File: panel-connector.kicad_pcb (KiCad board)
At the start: 2 copper layers, 95.9 x 90.2 mm, 25 parts, among them J1 PC104-8BIT, J10 CONN-TAB, J11 MOLEX_FFC-14, J12 CONN-TAB, J13 CONN-TAB, J14 CONN-TAB, J15 CONN-TAB, J16 MOLEX_FFC-14, J17 CONN-TAB, J18 CONN-TAB, J19 CONN-TAB, J2 PC104PTH, J20 CONN-TAB, J21 MOLEX_FFC-14, J22 CONN-TAB, J23 CONN-TAB, J24 CONN-TAB, J25 CONN-TAB, J3 PC104PTH, J4 PC104PTH, J5 PC104PTH, J6 MOLEX_FFC-14, J7 CONN-TAB, J8 CONN-TAB, J9 CONN-TAB

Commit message: Added mux
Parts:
- added 0.1uF1, 0.1uF2, 0.1uF3, 0.1uF4, C1, C2, C3, C4: C, Capacitors_SMD:C_0402, F.Cu at (55.9, 110.1)
- added R1, R10, R11, R12, R13, R14, R15, R16, R17, R18, R19, R2, R20, R23, R24, R27, R28, R3, R31, R32, R4, R5, R6, R7, R8, R9: R, Resistors_SMD:R_0402, F.Cu at (55.9, 110.1)
- added U1: ADG728, SFUSat:TSSOP-16, F.Cu at (39.7, 95.3)
- added U2: ADG728, SFUSat:TSSOP-16, F.Cu at (47.7, 95.3)
- added U3: ADG728, SFUSat:TSSOP-16, F.Cu at (55.7, 95.3)
- added U4: ADG728, SFUSat:TSSOP-16, F.Cu at (64.0, 95.3)

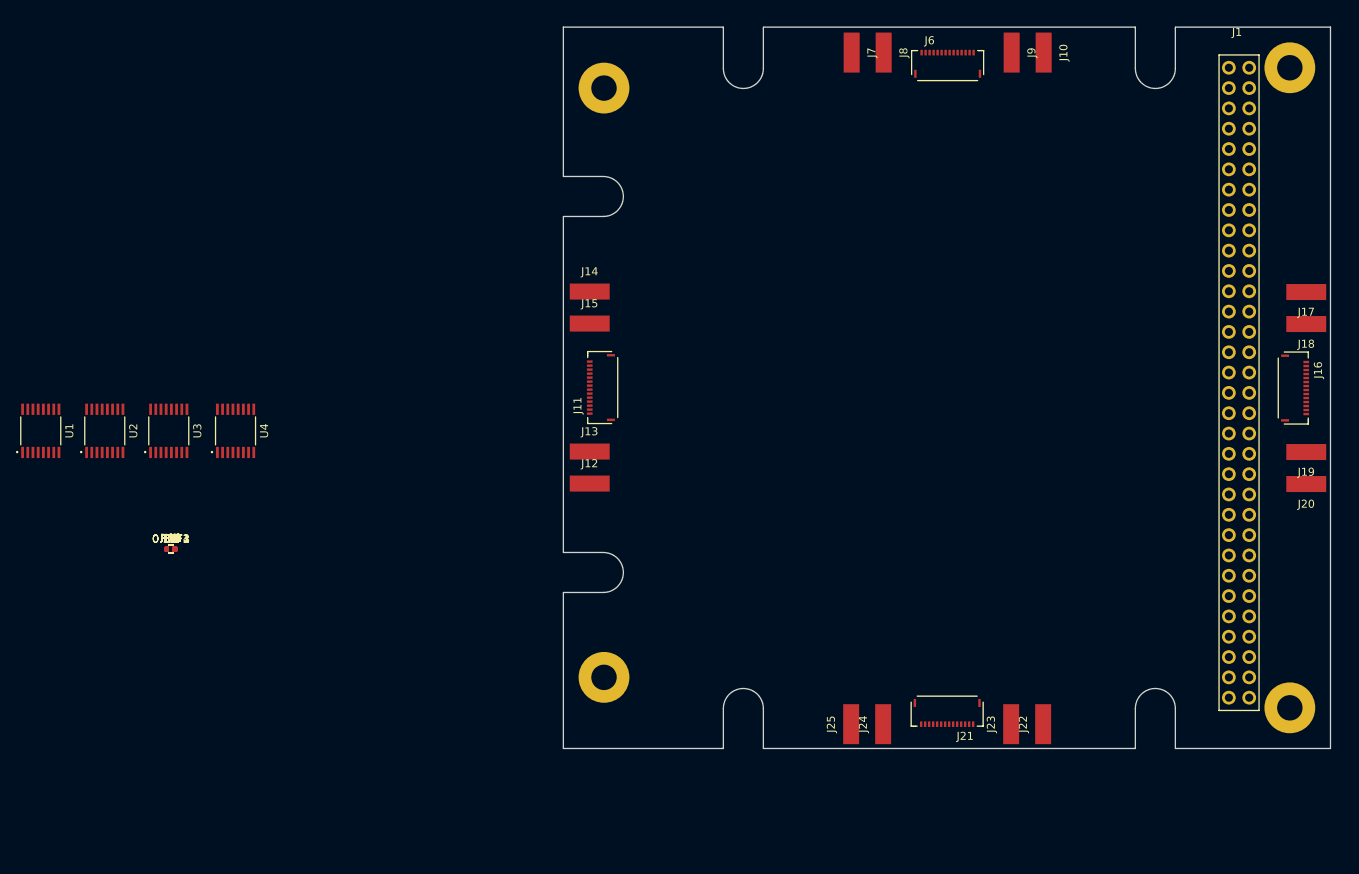
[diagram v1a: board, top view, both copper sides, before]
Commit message: Assigned some footprints and connected some nets
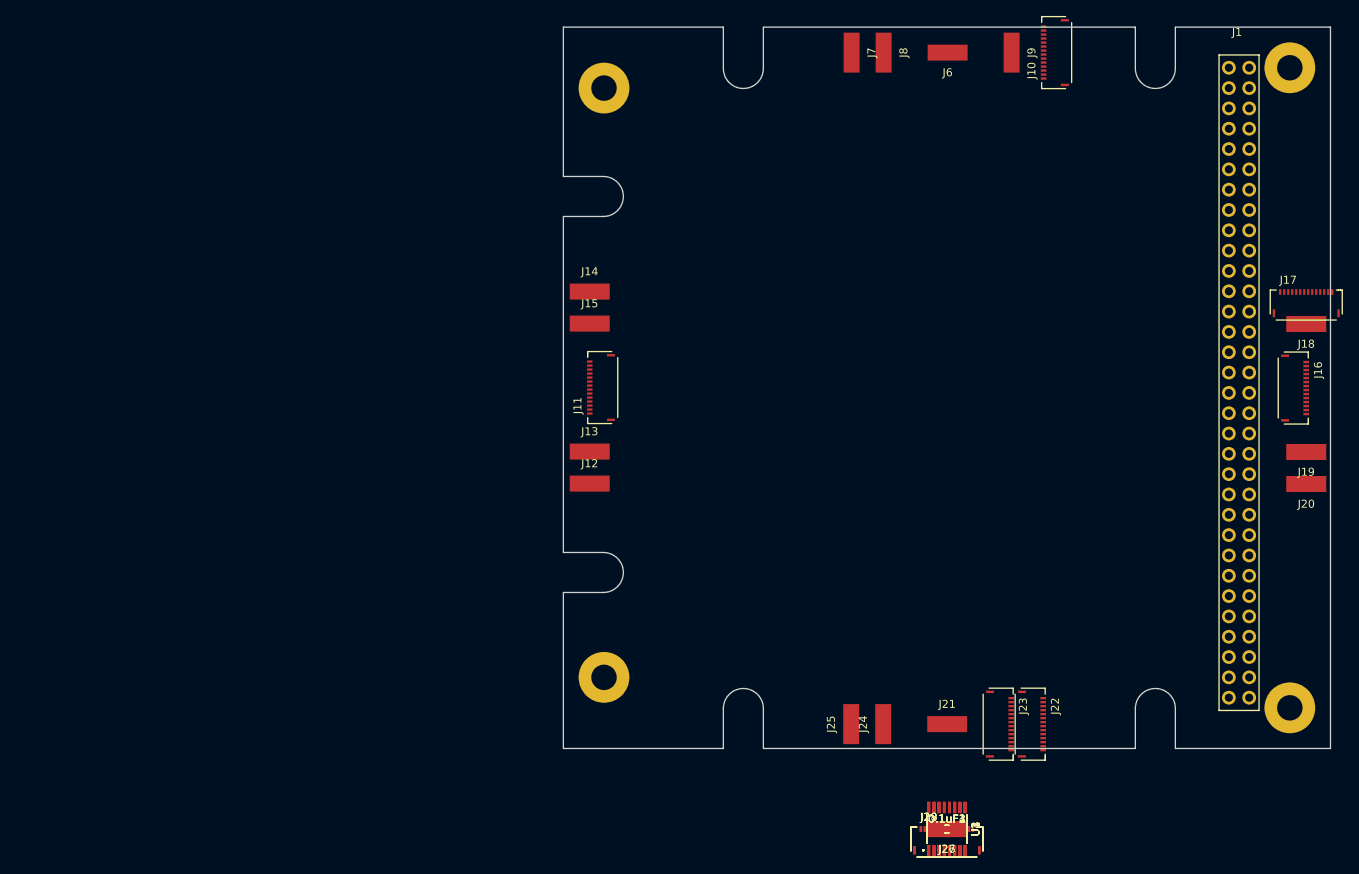
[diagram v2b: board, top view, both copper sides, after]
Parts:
- removed C1, C2, C3, C4: C, Capacitors_SMD:C_0402
- removed R1, R10, R11, R12, R13, R14, R15, R16, R17, R18, R19, R2, R20, R23, R24, R27, R28, R3, R31, R32, R4, R5, R6, R7, R8, R9: R, Resistors_SMD:R_0402
- added J26, J27: CONN-TAB, SFUSat:CONN_TAB, F.Cu at (152.9, 145.1)
- added J28, J29: MOLEX_FFC-14, SFUSat:MOLEX_FFC-14, F.Cu at (152.9, 145.1)
- J10, J17, J22, J23: value CONN-TAB -> MOLEX_FFC-14; footprint SFUSat:CONN_TAB -> SFUSat:MOLEX_FFC-14
- J21, J6: value MOLEX_FFC-14 -> CONN-TAB; footprint SFUSat:MOLEX_FFC-14 -> SFUSat:CONN_TAB
- moved U1 123.7 mm to (152.9, 145.1)
- moved U2 116.4 mm to (152.9, 145.1)
- moved U3 109.3 mm to (152.9, 145.1)
- moved 0.1uF1 103.1 mm to (152.9, 145.1)
- moved 0.1uF2 103.1 mm to (152.9, 145.1)
- moved 0.1uF3 103.1 mm to (152.9, 145.1)
- moved 0.1uF4 103.1 mm to (152.9, 145.1)
- moved U4 101.9 mm to (152.9, 145.1)

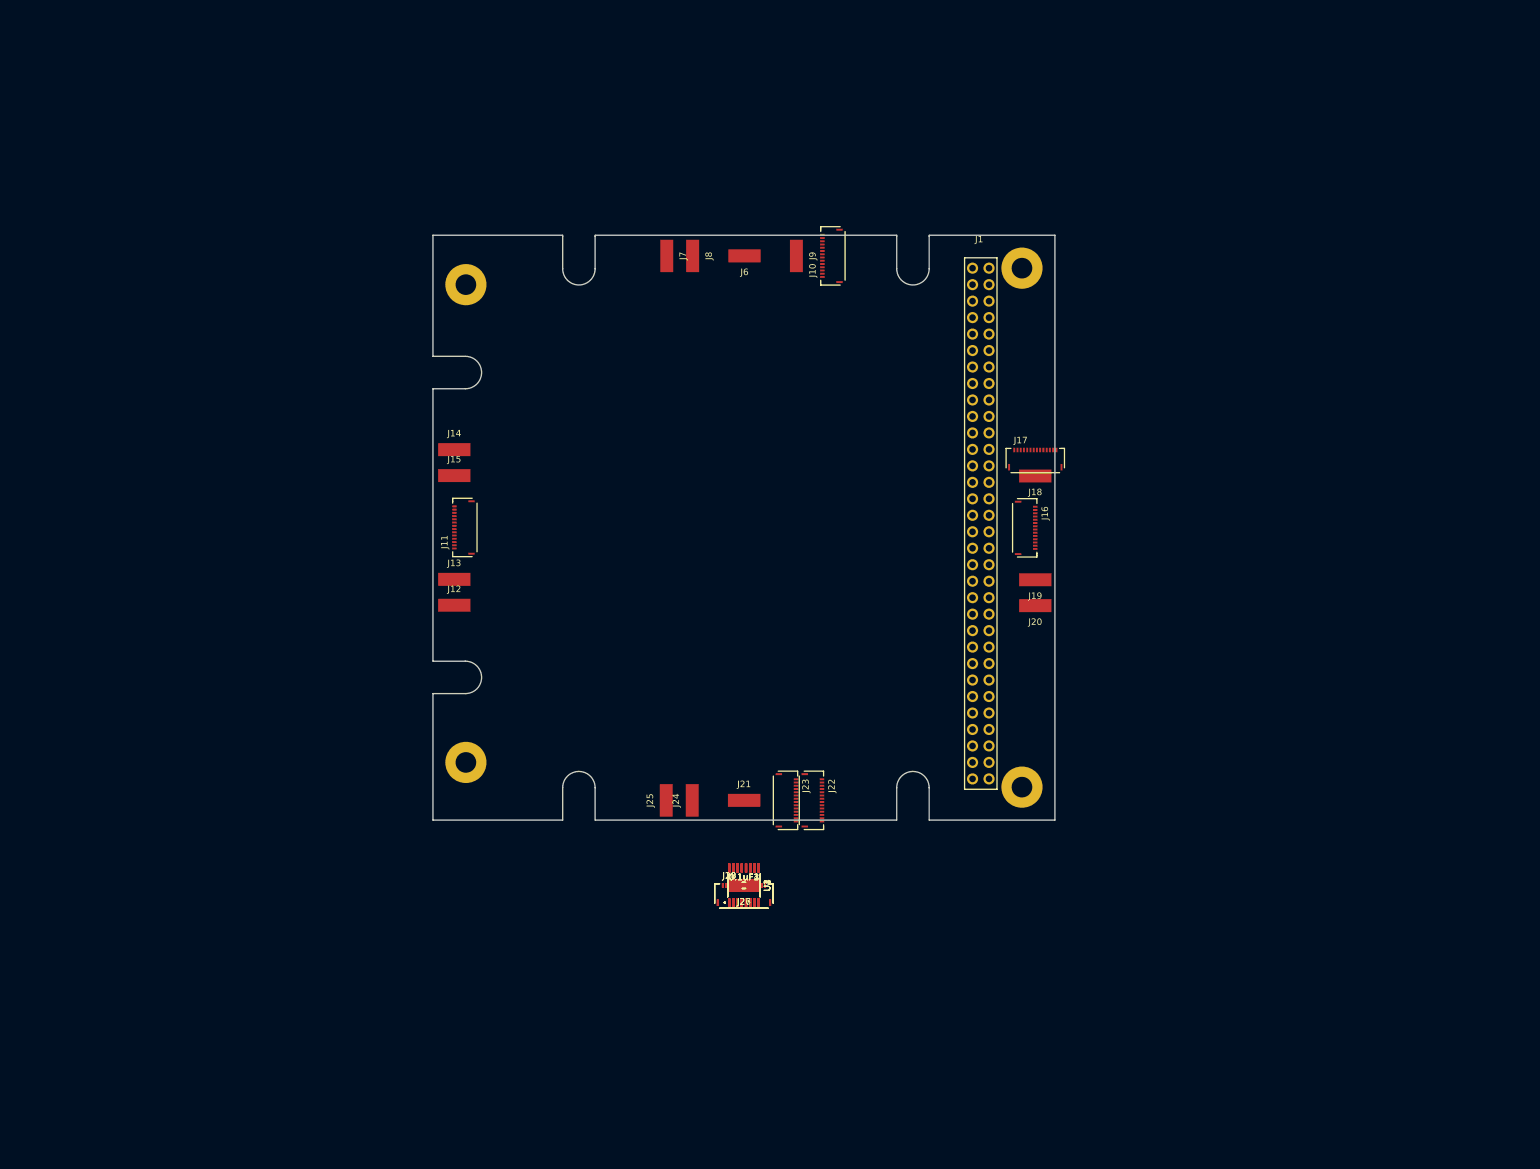
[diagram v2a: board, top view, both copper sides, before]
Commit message: Begand layout of connectors and added 3d models. The +Z connector will be placed only on the -X side of the board but because of the schematic hierarchy the net shows it is connected to all sides; ignore that for now. Connnected the sun sensor connector to mux according to systems spreadsheet, orientation does need checking.
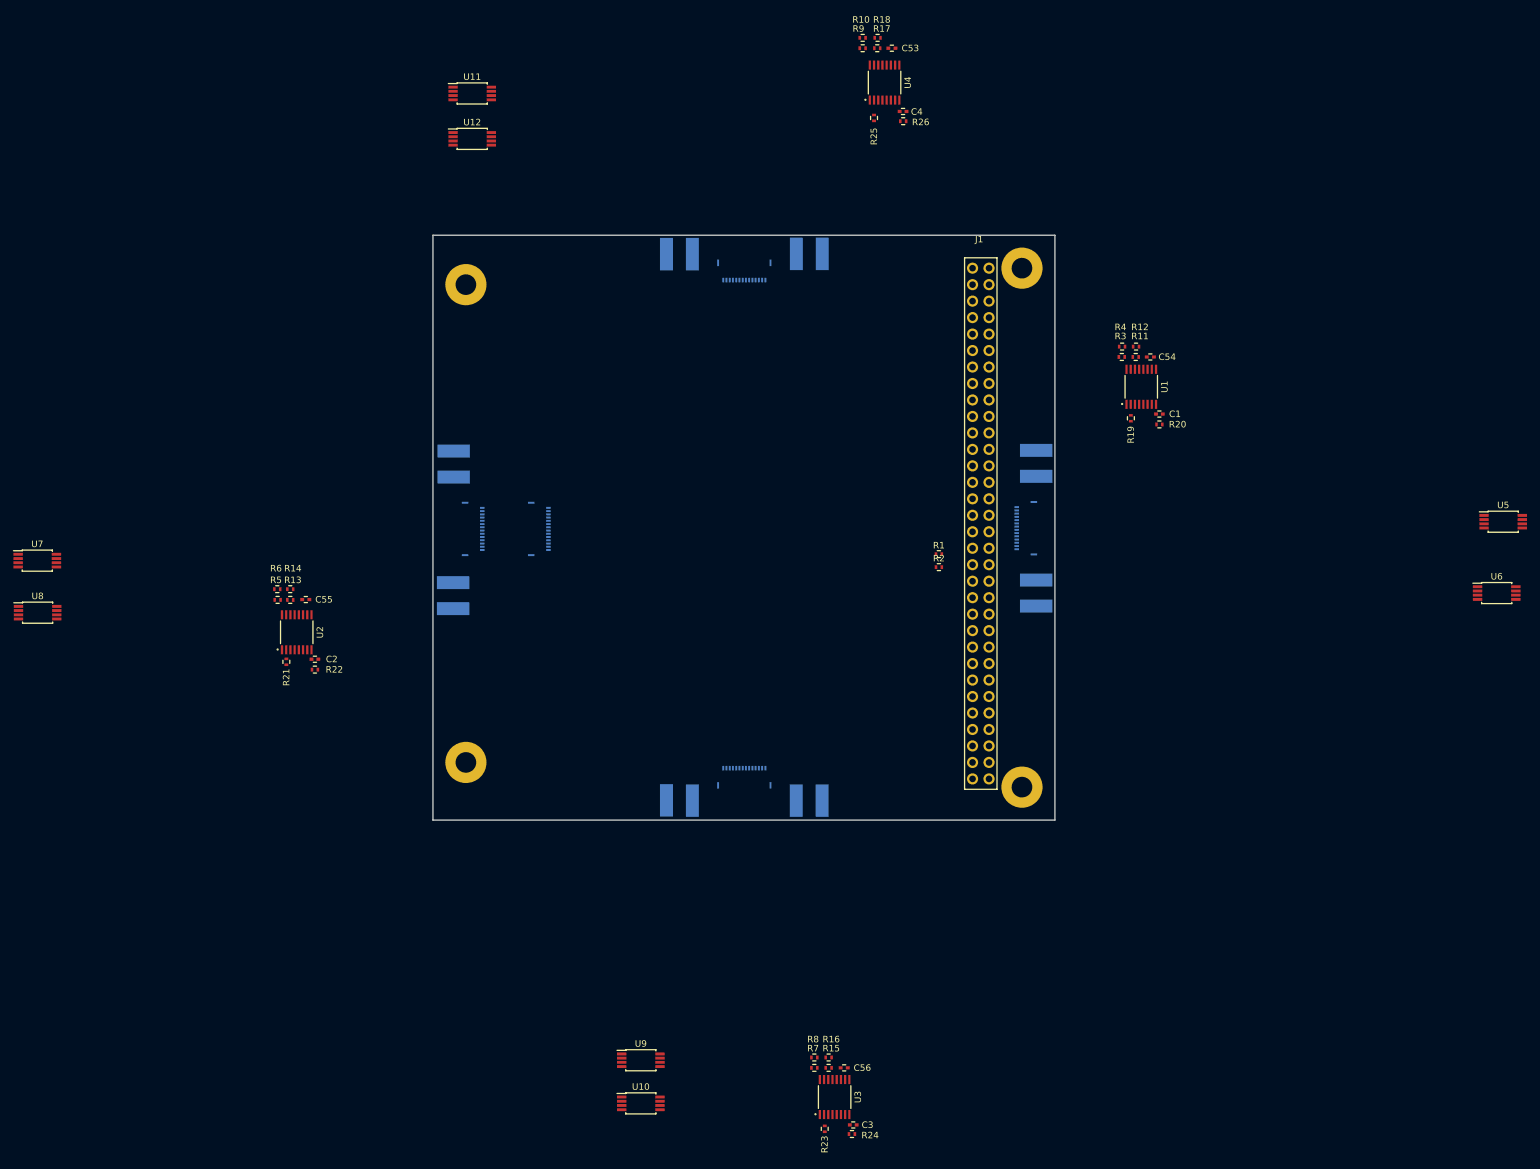
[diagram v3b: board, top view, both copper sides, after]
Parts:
- removed 0.1uF1, 0.1uF2, 0.1uF3, 0.1uF4: C, Capacitors_SMD:C_0402
- removed J17, J23, J29: MOLEX_FFC-14, SFUSat:MOLEX_FFC-14
- added C1: DNP, SFUSat:C_0402, F.Cu at (217.0, 72.4)
- added C2: DNP, SFUSat:C_0402, F.Cu at (86.8, 110.2)
- added C3: DNP, SFUSat:C_0402, F.Cu at (169.8, 182.0)
- added C4: DNP, SFUSat:C_0402, F.Cu at (177.5, 25.8)
- added C53: DNP, Capacitors_SMD:C_0402, F.Cu at (175.8, 16.0)
- added C54: DNP, Capacitors_SMD:C_0402, F.Cu at (215.6, 63.6)
- added C55: DNP, Capacitors_SMD:C_0402, F.Cu at (85.4, 101.0)
- added C56: DNP, Capacitors_SMD:C_0402, F.Cu at (168.4, 173.2)
- added R1: R, SFUSat:R_0402, F.Cu at (183.0, 94.0)
- added R10: DNP, SFUSat:R_0402, F.Cu at (171.2, 14.4)
- added R11: DNP, SFUSat:R_0402, F.Cu at (213.3, 63.6)
- added R12: 0R, SFUSat:R_0402, F.Cu at (213.4, 62.0)
- added R13: DNP, SFUSat:R_0402, F.Cu at (83.0, 101.0)
- added R14: 0R, SFUSat:R_0402, F.Cu at (83.0, 99.4)
- added R15: 0R, SFUSat:R_0402, F.Cu at (166.0, 173.2)
- added R16: DNP, SFUSat:R_0402, F.Cu at (166.0, 171.6)
- added R17: 0R, SFUSat:R_0402, F.Cu at (173.5, 16.0)
- added R18: DNP, SFUSat:R_0402, F.Cu at (173.6, 14.4)
- added R19: R, SFUSat:R_0402, F.Cu at (212.6, 73.0)
- added R2: R, SFUSat:R_0402, F.Cu at (183.0, 96.0)
- added R20: DNP, SFUSat:R_0402, F.Cu at (217.0, 74.0)
- added R21: R, SFUSat:R_0402, F.Cu at (82.4, 110.6)
- added R22: DNP, SFUSat:R_0402, F.Cu at (86.8, 111.8)
- added R23: R, SFUSat:R_0402, F.Cu at (165.4, 182.6)
- added R24: DNP, SFUSat:R_0402, F.Cu at (169.6, 183.4)
- added R25: R, SFUSat:R_0402, F.Cu at (173.0, 26.8)
- added R26: DNP, SFUSat:R_0402, F.Cu at (177.5, 27.2)
- added R3: DNP, SFUSat:R_0402, F.Cu at (211.2, 63.6)
- added R4: 0R, SFUSat:R_0402, F.Cu at (211.2, 62.0)
- added R5: 0R, SFUSat:R_0402, F.Cu at (81.0, 101.0)
- added R6: DNP, SFUSat:R_0402, F.Cu at (81.0, 99.4)
- added R7: DNP, SFUSat:R_0402, F.Cu at (163.8, 173.2)
- added R8: 0R, SFUSat:R_0402, F.Cu at (163.8, 171.6)
- added R9: 0R, SFUSat:R_0402, F.Cu at (171.2, 16.0)
- added U10: SPV1040, SFUSat:TSSOP-8_4.4x3mm_Pitch0.65mm, F.Cu at (137.1, 178.7)
- added U11: SPV1040, SFUSat:TSSOP-8_4.4x3mm_Pitch0.65mm, F.Cu at (111.0, 23.0)
- added U12: SPV1040, SFUSat:TSSOP-8_4.4x3mm_Pitch0.65mm, F.Cu at (111.0, 30.0)
- added U5: SPV1040, SFUSat:TSSOP-8_4.4x3mm_Pitch0.65mm, F.Cu at (270.0, 89.0)
- added U6: SPV1040, SFUSat:TSSOP-8_4.4x3mm_Pitch0.65mm, F.Cu at (269.0, 100.0)
- added U7: SPV1040, SFUSat:TSSOP-8_4.4x3mm_Pitch0.65mm, F.Cu at (44.0, 95.0)
- added U8: SPV1040, SFUSat:TSSOP-8_4.4x3mm_Pitch0.65mm, F.Cu at (44.0, 103.0)
- added U9: SPV1040, SFUSat:TSSOP-8_4.4x3mm_Pitch0.65mm, F.Cu at (137.1, 172.0)
- J10, J11, J12, J13, J14, J15, J16, J18, J19, J20, J21, J22, J24, J25, J26, J27, J28, J6, J7, J8, J9: moved to B.Cu
- moved U4 125.7 mm to (174.6, 21.3)
- moved U1 98.3 mm to (214.2, 68.2)
- moved J27 98.1 mm to (141.0, 47.7), turned to 90 degrees
- moved J26 97.7 mm to (145.0, 47.7), turned to 90 degrees
- moved J28 93.3 mm to (153.0, 51.7)
- moved J25 87.6 mm to (165.0, 47.7)
- moved J24 85.8 mm to (161.0, 47.7)
- moved J16 85.3 mm to (112.6, 90.1), turned to 90 degrees
- moved U2 79.2 mm to (84.0, 106.0)
- moved J7 75.8 mm to (198.0, 98.0), turned to 0 degrees
- moved J6 70.3 mm to (198.0, 102.0)
- moved J8 62.9 mm to (198.0, 82.0), turned to 0 degrees
- moved J20 60.8 mm to (145.0, 132.0), turned to 270 degrees
- moved J18 59.9 mm to (165.0, 132.0), turned to 270 degrees
- moved J10 51.6 mm to (195.0, 90.0), turned to 270 degrees
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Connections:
- J1 pad 17B: Net-(J1-Pad17B) -> /SDA
- J1 pad 18B: Net-(J1-Pad18B) -> /SCL
- J1 pad 1B: Net-(J1-Pad1B) -> GND
- J1 pad 23B: Net-(J1-Pad23B) -> /SENSOR_Y+
- J1 pad 24B: Net-(J1-Pad24B) -> /SENSOR_X-
- J1 pad 25B: Net-(J1-Pad25B) -> /SENSOR_Y-
- J1 pad 26B: Net-(J1-Pad26B) -> /SENSOR_X+
- J1 pad 32A: Net-(J1-Pad32A) -> GND
- J1 pad 32B: Net-(J1-Pad32B) -> GND
- J10 pad 1: Net-(J10-Pad1) -> /3V3
- J10 pad 10: Net-(J10-Pad10) -> /Port_X+/D6
- J10 pad 11: Net-(J10-Pad11) -> Z+D7
- J10 pad 12: Net-(J10-Pad12) -> Z+D8
- J10 pad 13: Net-(J10-Pad13) -> GND
- J10 pad 14: Net-(J10-Pad14) -> /3V3
- J10 pad 2: Net-(J10-Pad2) -> GND
- J10 pad 3: Net-(J10-Pad3) -> /Port_X+/D1
- J10 pad 4: Net-(J10-Pad4) -> /Port_X+/D2
- J10 pad 5: Net-(J10-Pad5) -> /Port_X+/D3
- J10 pad 6: Net-(J10-Pad6) -> /Port_X+/D4
- J10 pad 7: Net-(J10-Pad7) -> GND
- J10 pad 8: Net-(J10-Pad8) -> GND
- J10 pad 9: Net-(J10-Pad9) -> /Port_X+/D5
- J10 pad SHLD: Net-(J10-PadSHLD) -> GND
- J11 pad 1: Net-(J11-Pad1) -> /3V3
- J11 pad 11: Net-(J11-Pad11) -> Z+D7
- J11 pad 12: Net-(J11-Pad12) -> Z+D8
- J11 pad 13: Net-(J11-Pad13) -> GND
- J11 pad 14: Net-(J11-Pad14) -> /3V3
- J11 pad 2: Net-(J11-Pad2) -> GND
- J11 pad 7: Net-(J11-Pad7) -> GND
- J11 pad 8: Net-(J11-Pad8) -> GND
- J11 pad SHLD: Net-(J11-PadSHLD) -> GND
- J16 pad 1: Net-(J16-Pad1) -> /3V3
- J16 pad 10: Net-(J16-Pad10) -> /Port_X-/D6
- J16 pad 11: Net-(J16-Pad11) -> Z+D7
- J16 pad 12: Net-(J16-Pad12) -> Z+D8
- J16 pad 13: Net-(J16-Pad13) -> GND
- J16 pad 14: Net-(J16-Pad14) -> /3V3
- J16 pad 2: Net-(J16-Pad2) -> GND
- J16 pad 3: Net-(J16-Pad3) -> /Port_X-/D1
- J16 pad 4: Net-(J16-Pad4) -> /Port_X-/D2
- J16 pad 5: Net-(J16-Pad5) -> /Port_X-/D3
- J16 pad 6: Net-(J16-Pad6) -> /Port_X-/D4
- J16 pad 7: Net-(J16-Pad7) -> GND
- J16 pad 8: Net-(J16-Pad8) -> GND
- J16 pad 9: Net-(J16-Pad9) -> /Port_X-/D5
- J16 pad SHLD: Net-(J16-PadSHLD) -> GND
- J2 pad 1: Net-(J2-Pad1) -> GND
- J22 pad 1: Net-(J22-Pad1) -> /3V3
- J22 pad 10: Net-(J22-Pad10) -> /Port_Y+/D6
- J22 pad 11: Net-(J22-Pad11) -> Z+D7
- J22 pad 12: Net-(J22-Pad12) -> Z+D8
- J22 pad 13: Net-(J22-Pad13) -> GND
- J22 pad 14: Net-(J22-Pad14) -> /3V3
- J22 pad 2: Net-(J22-Pad2) -> GND
- J22 pad 3: Net-(J22-Pad3) -> /Port_Y+/D1
- J22 pad 4: Net-(J22-Pad4) -> /Port_Y+/D2
- J22 pad 5: Net-(J22-Pad5) -> /Port_Y+/D3
- J22 pad 6: Net-(J22-Pad6) -> /Port_Y+/D4
- J22 pad 7: Net-(J22-Pad7) -> GND
- J22 pad 8: Net-(J22-Pad8) -> GND
- J22 pad 9: Net-(J22-Pad9) -> /Port_Y+/D5
- J22 pad SHLD: Net-(J22-PadSHLD) -> GND
- J28 pad 1: Net-(J28-Pad1) -> /3V3
- J28 pad 10: Net-(J28-Pad10) -> /Port_Y-/D6
- J28 pad 11: Net-(J28-Pad11) -> Z+D7
- J28 pad 12: Net-(J28-Pad12) -> Z+D8
- J28 pad 13: Net-(J28-Pad13) -> GND
- J28 pad 14: Net-(J28-Pad14) -> /3V3
- J28 pad 2: Net-(J28-Pad2) -> GND
- J28 pad 3: Net-(J28-Pad3) -> /Port_Y-/D1
- J28 pad 4: Net-(J28-Pad4) -> /Port_Y-/D2
- J28 pad 5: Net-(J28-Pad5) -> /Port_Y-/D3
- J28 pad 6: Net-(J28-Pad6) -> /Port_Y-/D4
- J28 pad 7: Net-(J28-Pad7) -> GND
- J28 pad 8: Net-(J28-Pad8) -> GND
- J28 pad 9: Net-(J28-Pad9) -> /Port_Y-/D5
- J28 pad SHLD: Net-(J28-PadSHLD) -> GND
- J3 pad 1: Net-(J3-Pad1) -> GND
- J4 pad 1: Net-(J4-Pad1) -> GND
- J5 pad 1: Net-(J5-Pad1) -> GND
- U1 pad 1: /Port_X+/SCL -> /SCL
- U1 pad 10: Net-(U1-Pad10) -> Z+D7
- U1 pad 11: Net-(U1-Pad11) -> /Port_X+/D6
- U1 pad 12: Net-(U1-Pad12) -> /Port_X+/D5
- U1 pad 13: /Port_X+/3V3 -> /3V3
- U1 pad 3: /Port_X+/SDA -> /SDA
- U1 pad 4: Net-(U1-Pad4) -> /Port_X+/D1
- U1 pad 5: Net-(U1-Pad5) -> /Port_X+/D2
- U1 pad 6: Net-(U1-Pad6) -> /Port_X+/D3
- U1 pad 7: Net-(U1-Pad7) -> /Port_X+/D4
- U1 pad 8: /Port_X+/SUN_SENSOR -> /SENSOR_X+
- U1 pad 9: Net-(U1-Pad9) -> Z+D8
- U2 pad 1: /Port_X-/SCL -> /SCL
- U2 pad 10: Net-(U2-Pad10) -> Z+D7
- U2 pad 11: Net-(U2-Pad11) -> /Port_X-/D6
- U2 pad 12: Net-(U2-Pad12) -> /Port_X-/D5
- U2 pad 13: /Port_X-/3V3 -> /3V3
- U2 pad 3: /Port_X-/SDA -> /SDA
- U2 pad 4: Net-(U2-Pad4) -> /Port_X-/D1
- U2 pad 5: Net-(U2-Pad5) -> /Port_X-/D2
- U2 pad 6: Net-(U2-Pad6) -> /Port_X-/D3
- U2 pad 7: Net-(U2-Pad7) -> /Port_X-/D4
- U2 pad 8: /Port_X-/SUN_SENSOR -> /SENSOR_X-
- U2 pad 9: Net-(U2-Pad9) -> Z+D8
- U3 pad 1: /Port_Y+/SCL -> /SCL
- U3 pad 10: Net-(U3-Pad10) -> Z+D7
- U3 pad 11: Net-(U3-Pad11) -> /Port_Y+/D6
- U3 pad 12: Net-(U3-Pad12) -> /Port_Y+/D5
- U3 pad 13: /Port_Y+/3V3 -> /3V3
- U3 pad 3: /Port_Y+/SDA -> /SDA
- U3 pad 4: Net-(U3-Pad4) -> /Port_Y+/D1
- U3 pad 5: Net-(U3-Pad5) -> /Port_Y+/D2
- U3 pad 6: Net-(U3-Pad6) -> /Port_Y+/D3
- U3 pad 7: Net-(U3-Pad7) -> /Port_Y+/D4
- U3 pad 8: /Port_Y+/SUN_SENSOR -> /SENSOR_Y+
- U3 pad 9: Net-(U3-Pad9) -> Z+D8
- U4 pad 1: /Port_Y-/SCL -> /SCL
- U4 pad 10: Net-(U4-Pad10) -> Z+D7
- U4 pad 11: Net-(U4-Pad11) -> /Port_Y-/D6
- U4 pad 12: Net-(U4-Pad12) -> /Port_Y-/D5
- U4 pad 13: /Port_Y-/3V3 -> /3V3
- U4 pad 3: /Port_Y-/SDA -> /SDA
- U4 pad 4: Net-(U4-Pad4) -> /Port_Y-/D1
- U4 pad 5: Net-(U4-Pad5) -> /Port_Y-/D2
- U4 pad 6: Net-(U4-Pad6) -> /Port_Y-/D3
- U4 pad 7: Net-(U4-Pad7) -> /Port_Y-/D4
- U4 pad 8: /Port_Y-/SUN_SENSOR -> /SENSOR_Y-
- U4 pad 9: Net-(U4-Pad9) -> Z+D8
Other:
- outline, holes or cut-outs redrawn
- rule pad_to_mask_clearance: 0.2 -> 0
- board text added: "X+"
- board text added: "X-"
- board text added: "Y+"
- board text added: "Y-"
- board text added: "Z+"
